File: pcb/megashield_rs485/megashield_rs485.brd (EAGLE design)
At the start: 101.6 x 53.3 mm, 16 parts, among them J11 DYNAMIXEL_RS485, U1 SN75176B

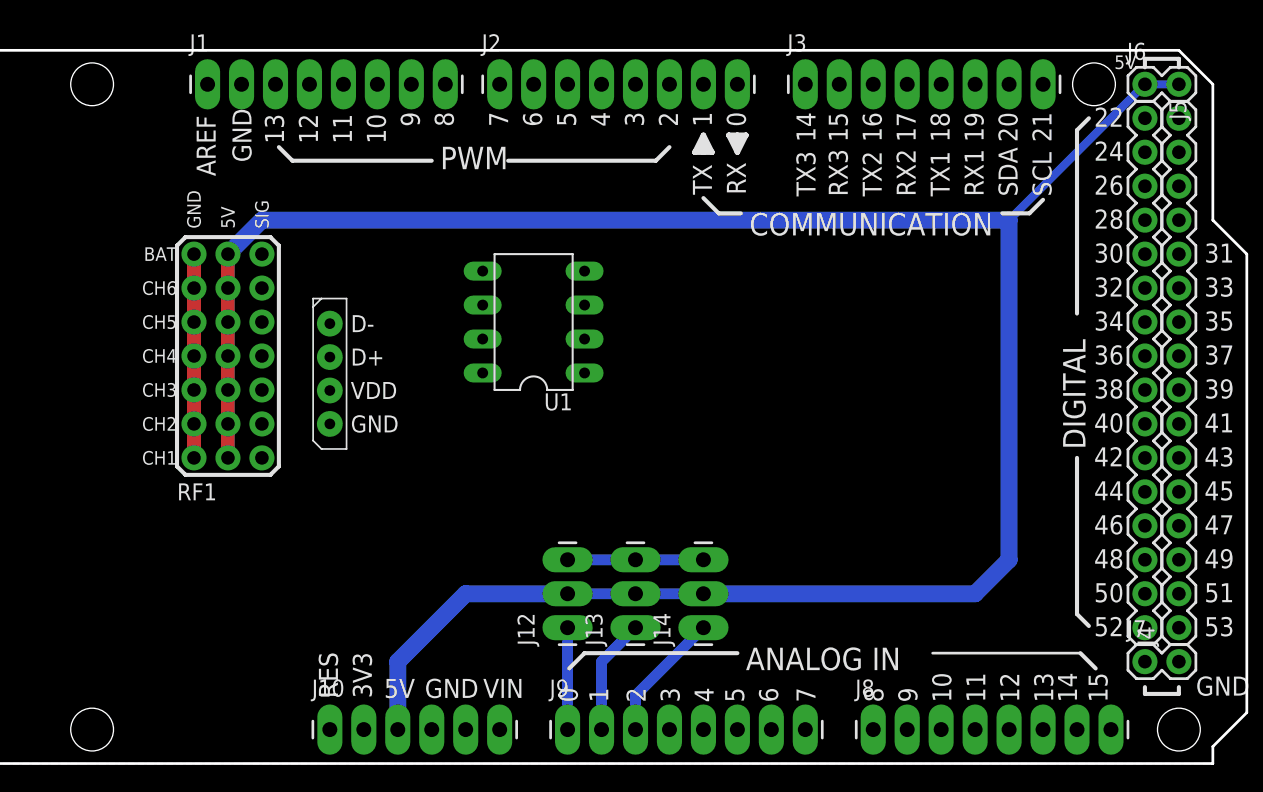
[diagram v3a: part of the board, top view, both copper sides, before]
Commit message: PCB con elementos para conexion de pantalla
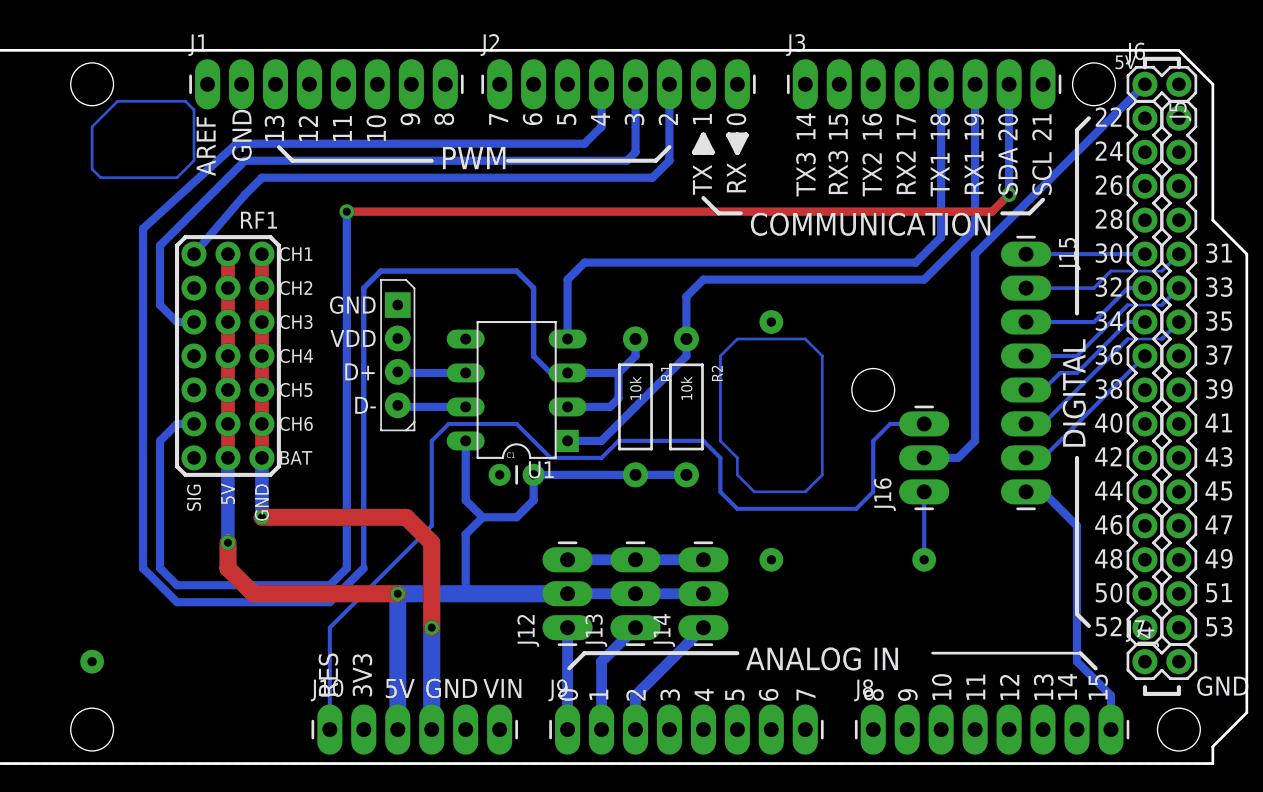
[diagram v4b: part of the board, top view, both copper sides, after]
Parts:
- added C1: 0.1u, mecatronica_eagle_lib:CAP-PTH-SMALL
- added J15: (no value), mecatronica_eagle_lib:1X08_LONGPADS
- added J16: (no value), mecatronica_eagle_lib:1X03_LONGPADS
- added R1, R2: 10k, mecatronica_eagle_lib:AXIAL-0.4
- U1: value SN75176B -> RS485
- moved RF1 16.1 mm to (27.9, 22.9), turned to 180 degrees
- moved J11 10.2 mm to (38.1, 34.3), turned to 270 degrees
- moved U1 5.24 mm to (47.0, 27.9)
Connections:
- net D14 renamed D21
- net D18 renamed RX2
- net D19 renamed TX2
- net SCL renamed TX3
- net SDA renamed RX3
- removed net D15: J3.7
- removed net D16: J3.6
- removed net D17: J3.5
- removed net N$3: RF1.CH1
- removed net N$5: RF1.CH3
- removed net N$8: RF1.CH6
- new net 5V@1: J16.2, J6.1, J6.2
- new net D20: J3.7, RF1.CH6
- new net N$1: J11.3, U1.6
- new net N$2: J11.4, U1.7
- new net RX1: J3.6, R2.P$1, U1.1
- new net TX0: J2.7
- net 5V: now also C1.2, R1.P$2, R2.P$2, U1.8; no longer J6.1, J6.2
- net A15: now also J15.8
- net AREF: now also J1.1; no longer J1.8
- net D10: now also J1.6; no longer J1.3
- net D11: now also J1.5; no longer J1.4
- net D12: now also J1.4; no longer J1.5
- net D13: now also J1.3; no longer J1.6
- net D2: now also J2.6, RF1.CH1; no longer J2.3
- net D3: now also J2.5, RF1.CH3; no longer J2.4
- net D30: now also J15.1
- net D31: now also J15.2
- net D32: now also J15.3
- net D33: now also J15.4
- net D34: now also J15.5
- net D35: now also J15.6
- net D36: now also J15.7
- net D4: now also J2.4, R1.P$1, U1.2, U1.3; no longer J2.5
- net D5: now also J2.3; no longer J2.6
- net D6: now also J2.2; no longer J2.7
- net D7: now also J2.1; no longer J2.8
- net D8: now also J1.8; no longer J1.1
- net D9: now also J1.7; no longer J1.2
- net GND: now also C1.1, J1.2, J16.1, U1.5; no longer J1.7
- net RES: now also J16.3
- net RX0: now also J2.8; no longer J2.1
- net TX1: now also J3.5, U1.4; no longer J2.2
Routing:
- net D4: track 0.00 -> 140.2 mm
- net D20: track 0.00 -> 112.6 mm, vias 0 -> 2
- net RES: track 0.00 -> 72.1 mm
- net 5V: track 155.7 -> 84.9 mm, vias 0 -> 2
- net D3: track 0.00 -> 51.0 mm
- net RX1: track 0.00 -> 50.5 mm
- net TX1: track 0.00 -> 45.1 mm
- net D2: track 0.00 -> 44.4 mm
- net GND: track 10.2 -> 47.1 mm, vias 0 -> 6
- net 5V@1: track 0.00 -> 36.3 mm
- net N$3: track 0.00 -> 34.4 mm
- net N$5: track 0.00 -> 24.1 mm
- net A15: track 0.00 -> 21.2 mm
- net D35: track 0.00 -> 14.6 mm
- net D33: track 0.00 -> 13.5 mm
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
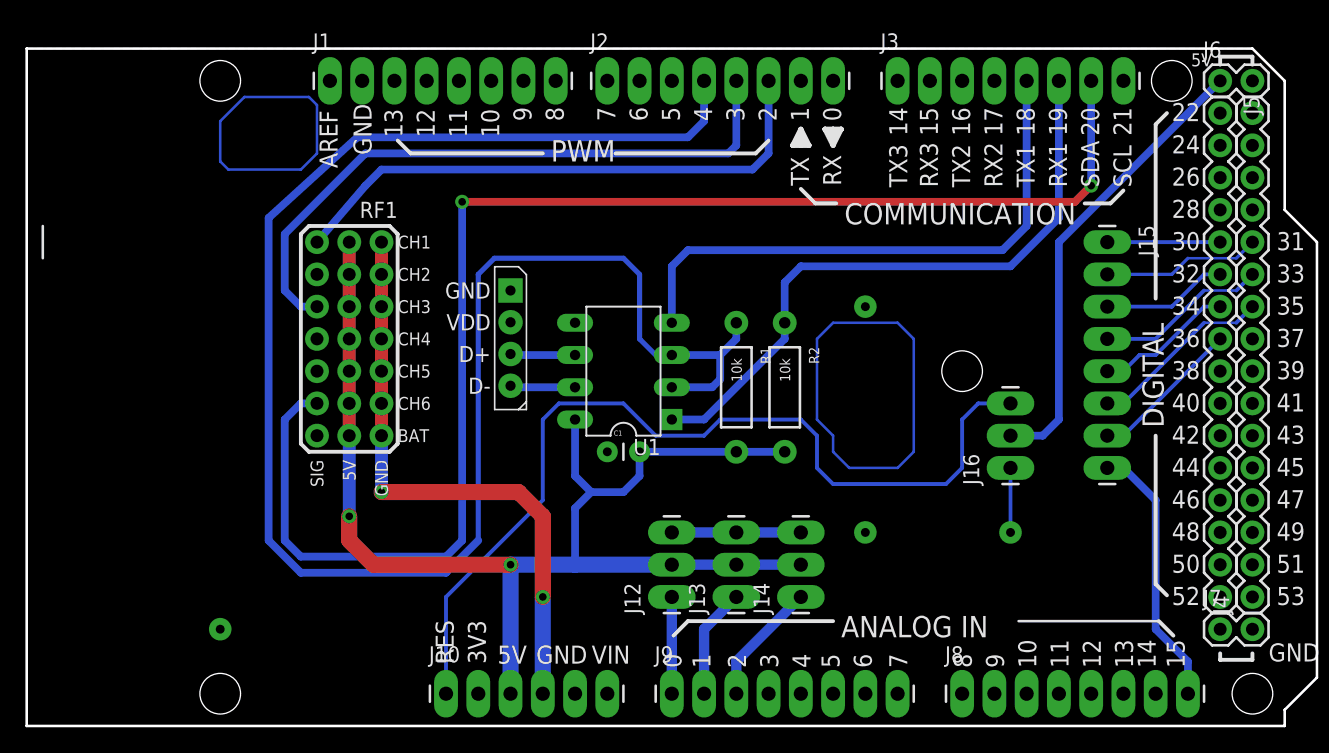
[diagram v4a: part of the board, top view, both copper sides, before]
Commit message: Basic example using serial interface
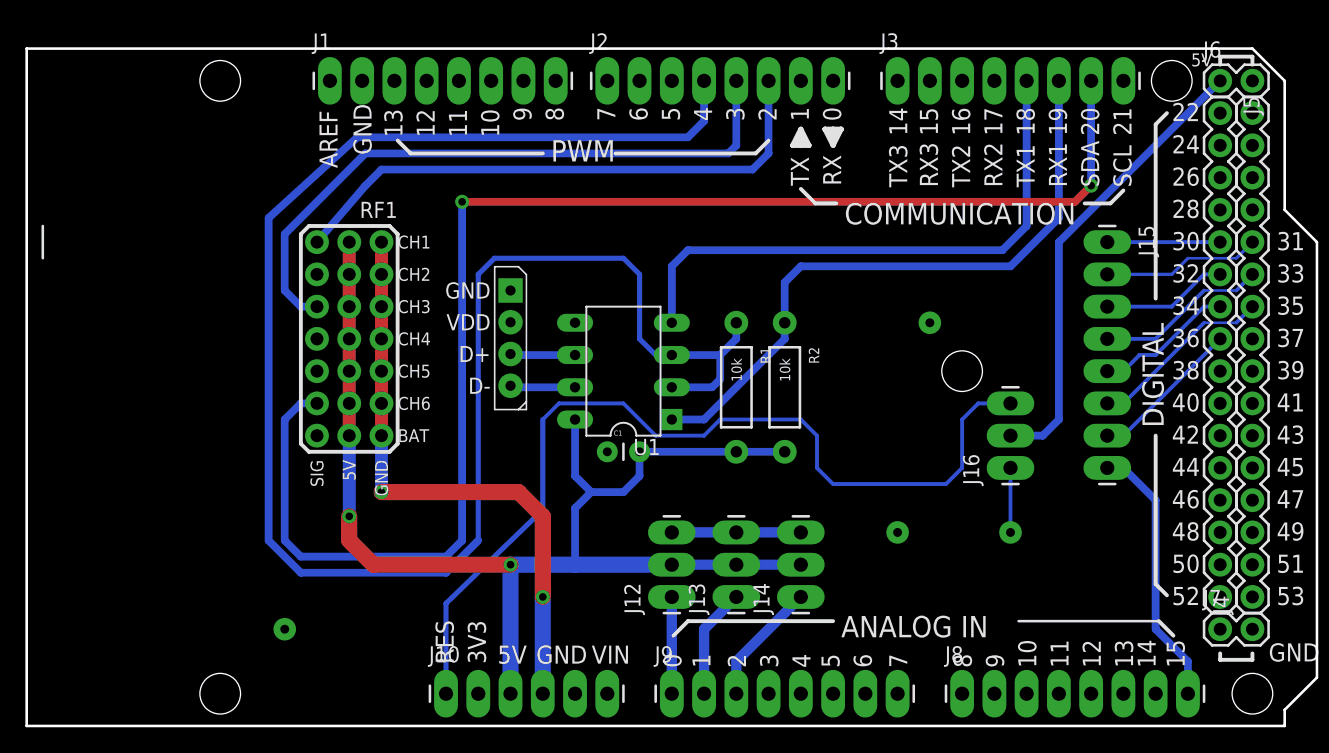
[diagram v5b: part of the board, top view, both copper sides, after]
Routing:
- net N$3: track 34.4 -> 0.00 mm
- net N$5: track 24.1 -> 0.00 mm
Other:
- board text added: "PWR"
- board text added: "USB"
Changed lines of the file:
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@@
 <setting verticaltext="up"/>
 </settings>
-<grid distance="25" unitdist="mil" unit="mil" style="lines" multiple="1" display="yes" altdistance="50" altunitdist="mil" altunit="mil"/>
+<grid distance="50" unitdist="mil" unit="mil" style="lines" multiple="1" display="yes" altdistance="50" altunitdist="mil" altunit="mil"/>
 <layers>
 <layer number="1" name="Top" color="4" fill="1" visible="yes" active="yes"/>
@@
 <layer number="23" name="tOrigins" color="15" fill="1" visible="yes" active="yes"/>
 <layer number="24" name="bOrigins" color="15" fill="1" visible="yes" active="yes"/>
-<layer number="25" name="tNames" color="7" fill="1" visible="no" active="yes"/>
+<layer number="25" name="tNames" color="7" fill="1" visible="yes" active="yes"/>
 <layer number="26" name="bNames" color="7" fill="1" visible="yes" active="yes"/>
 <layer number="27" name="tValues" color="7" fill="1" visible="yes" active="yes"/>
@@
 <layer number="43" name="vRestrict" color="2" fill="10" visible="no" active="yes"/>
 <layer number="44" name="Drills" color="7" fill="1" visible="no" active="yes"/>
-<layer number="45" name="Holes" color="7" fill="1" visible="yes" active="yes"/>
+<layer number="45" name="Holes" color="7" fill="1" visible="no" active="yes"/>
 <layer number="46" name="Milling" color="3" fill="1" visible="no" active="yes"/>
 <layer number="47" name="Measures" color="7" fill="1" visible="no" active="yes"/>
@@
 <hole x="96.52" y="2.54" drill="3.2"/>
 <hole x="73.66" y="27.94" drill="3.2"/>
+<rectangle x1="62.23" y1="24.13" x2="67.31" y2="31.75" layer="42"/>
+<rectangle x1="14.732" y1="43.942" x2="21.844" y2="48.514" layer="42"/>
+<wire x1="-6.35" y1="44.196" x2="9.906" y2="44.196" width="0.4064" layer="51"/>
+<wire x1="9.906" y1="44.196" x2="9.906" y2="32.004" width="0.4064" layer="51"/>
+<wire x1="9.906" y1="32.004" x2="-6.35" y2="32.004" width="0.4064" layer="51"/>
+<wire x1="-6.35" y1="32.004" x2="-6.35" y2="44.196" width="0.4064" layer="51"/>
+<text x="-1.524" y="37.084" size="2.54" layer="51">USB</text>
+<wire x1="-2.032" y1="12.192" x2="11.684" y2="12.192" width="0.4064" layer="51"/>
+<wire x1="11.684" y1="12.192" x2="11.684" y2="2.794" width="0.4064" layer="51"/>
+<wire x1="11.684" y1="2.794" x2="-2.032" y2="2.794" width="0.4064" layer="51"/>
+<wire x1="-2.032" y1="2.794" x2="-2.032" y2="12.192" width="0.4064" layer="51"/>
+<text x="1.524" y="6.35" size="2.54" layer="51">PWR</text>
+<rectangle x1="0" y1="30.48" x2="11.43" y2="53.34" layer="42"/>
+<rectangle x1="0" y1="0" x2="15.24" y2="13.97" layer="42"/>
 </plain>
 <attributes>
@@
 </class>
 </classes>
-<designrules name="config_through_hole *">
-<description language="en">&lt;b&gt;EAGLE Design Rules&lt;/b&gt;
-&lt;p&gt;
-The default Design Rules have been set to cover
-a wide range of applications. Your particular design
-may have different requirements, so please make the
-necessary adjustments and save your customized
-design rules under a new name.</description>
+<designrules name="config_through_hole">
+<description language="en">&lt;b&gt;Mecatronica default rules&lt;/b&gt;
+</description>
 <param name="layerSetup" value="(1*16)"/>
 <param name="mtCopper" value="0.035mm 0.035mm 0.035mm 0.035mm 0.035mm 0.035mm 0.035mm 0.035mm 0.035mm 0.035mm 0.035mm 0.035mm 0.035mm 0.035mm 0.035mm 0.035mm"/>
@@
 <param name="srMaxRoundness" value="0mil"/>
 <param name="slThermalIsolate" value="10mil"/>
-<param name="slThermalsForVias" value="0"/>
+<param name="slThermalsForVias" value="1"/>
 <param name="dpMaxLengthDifference" value="10mm"/>
 <param name="dpGapFactor" value="2.5"/>
@@
 <contactref element="J10" pad="1"/>
 <contactref element="J16" pad="3"/>
-<wire x1="33.02" y1="2.54" x2="33.02" y2="10.16" width="0.3048" layer="16"/>
-<wire x1="33.02" y1="10.16" x2="40.64" y2="17.78" width="0.3048" layer="16"/>
-<wire x1="40.64" y1="17.78" x2="40.64" y2="24.13" width="0.3048" layer="16"/>
+<wire x1="33.02" y1="2.54" x2="33.02" y2="9.652" width="0.4064" layer="16"/>
+<wire x1="33.02" y1="9.652" x2="40.64" y2="17.018" width="0.4064" layer="16"/>
+<wire x1="40.64" y1="17.018" x2="40.64" y2="24.13" width="0.4064" layer="16"/>
 <wire x1="40.64" y1="24.13" x2="41.91" y2="25.4" width="0.3048" layer="16"/>
 <wire x1="41.91" y1="25.4" x2="46.99" y2="25.4" width="0.3048" layer="16"/>
@@
 <vertex x="99.06" y="50.8"/>
 <vertex x="96.52" y="53.34"/>
+<vertex x="21.971" y="53.34"/>
 <vertex x="0" y="53.34"/>
-<vertex x="0" y="2.54"/>
 </polygon>
 <polygon width="0.2032" layer="1" isolate="0.3048">
@@
 <via x="40.64" y="10.16" extent="1-16" drill="0.6" shape="square"/>
 <wire x1="27.94" y1="18.415" x2="27.94" y2="22.86" width="1.016" layer="16"/>
-<via x="15.24" y="7.62" extent="1-16" drill="0.7" diameter="1.778" shape="square"/>
-<via x="66.04" y="15.24" extent="1-16" drill="0.7" diameter="1.778" shape="square"/>
+<via x="20.32" y="7.62" extent="1-16" drill="0.7" diameter="1.778" shape="square"/>
+<via x="68.58" y="15.24" extent="1-16" drill="0.7" diameter="1.778" shape="square"/>
 <via x="77.47" y="15.24" extent="1-16" drill="0.7" diameter="1.778" shape="square"/>
-<via x="66.04" y="33.02" extent="1-16" drill="0.7" diameter="1.778" shape="square"/>
+<via x="71.12" y="31.75" extent="1-16" drill="0.7" diameter="1.778" shape="square"/>
 <contactref element="J16" pad="1"/>
 <wire x1="77.47" y1="20.32" x2="77.47" y2="15.24" width="0.3048" layer="16"/>
@@
 <wire x1="93.98" y1="50.8" x2="96.52" y2="50.8" width="0" layer="19" extent="1-1"/>
 </signal>
-<signal name="N$3">
-<wire x1="68.58" y1="31.75" x2="69.85" y2="30.48" width="0.2032" layer="16"/>
-<wire x1="69.85" y1="30.48" x2="69.85" y2="21.59" width="0.2032" layer="16"/>
-<wire x1="62.23" y1="24.13" x2="62.23" y2="30.48" width="0.2032" layer="16"/>
-<wire x1="62.23" y1="30.48" x2="63.5" y2="31.75" width="0.2032" layer="16"/>
-<wire x1="63.5" y1="31.75" x2="68.58" y2="31.75" width="0.2032" layer="16"/>
-<wire x1="62.23" y1="24.13" x2="63.5" y2="22.86" width="0.2032" layer="16"/>
-<wire x1="63.5" y1="22.86" x2="63.5" y2="21.59" width="0.2032" layer="16"/>
-<wire x1="63.5" y1="21.59" x2="64.77" y2="20.32" width="0.2032" layer="16"/>
-<wire x1="64.77" y1="20.32" x2="68.58" y2="20.32" width="0.2032" layer="16"/>
-<wire x1="68.58" y1="20.32" x2="69.85" y2="21.59" width="0.2032" layer="16"/>
-</signal>
-<signal name="N$5">
-<wire x1="17.145" y1="49.53" x2="22.225" y2="49.53" width="0.2032" layer="16"/>
-<wire x1="22.225" y1="49.53" x2="22.86" y2="48.895" width="0.2032" layer="16"/>
-<wire x1="22.86" y1="48.895" x2="22.86" y2="45.085" width="0.2032" layer="16"/>
-<wire x1="22.86" y1="45.085" x2="21.59" y2="43.815" width="0.2032" layer="16"/>
-<wire x1="21.59" y1="43.815" x2="15.875" y2="43.815" width="0.2032" layer="16"/>
-<wire x1="15.875" y1="43.815" x2="15.24" y2="44.45" width="0.2032" layer="16"/>
-<wire x1="15.24" y1="44.45" x2="15.24" y2="47.625" width="0.2032" layer="16"/>
-<wire x1="15.24" y1="47.625" x2="17.145" y2="49.53" width="0.2032" layer="16"/>
-</signal>
 </signals>
